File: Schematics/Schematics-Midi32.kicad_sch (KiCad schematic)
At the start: 1 part, among them J1 AudioJack2

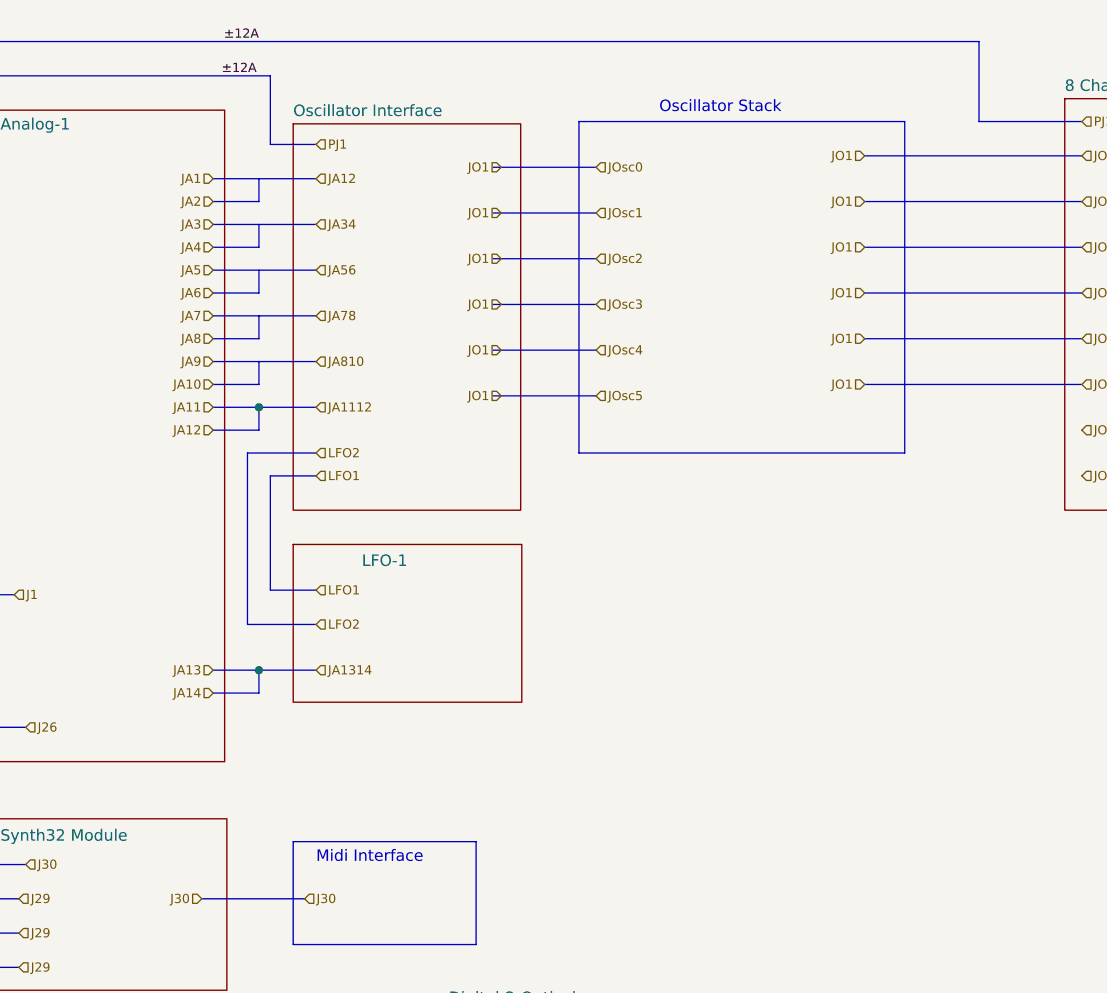
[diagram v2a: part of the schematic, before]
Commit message: Noise generator and experimental steups.
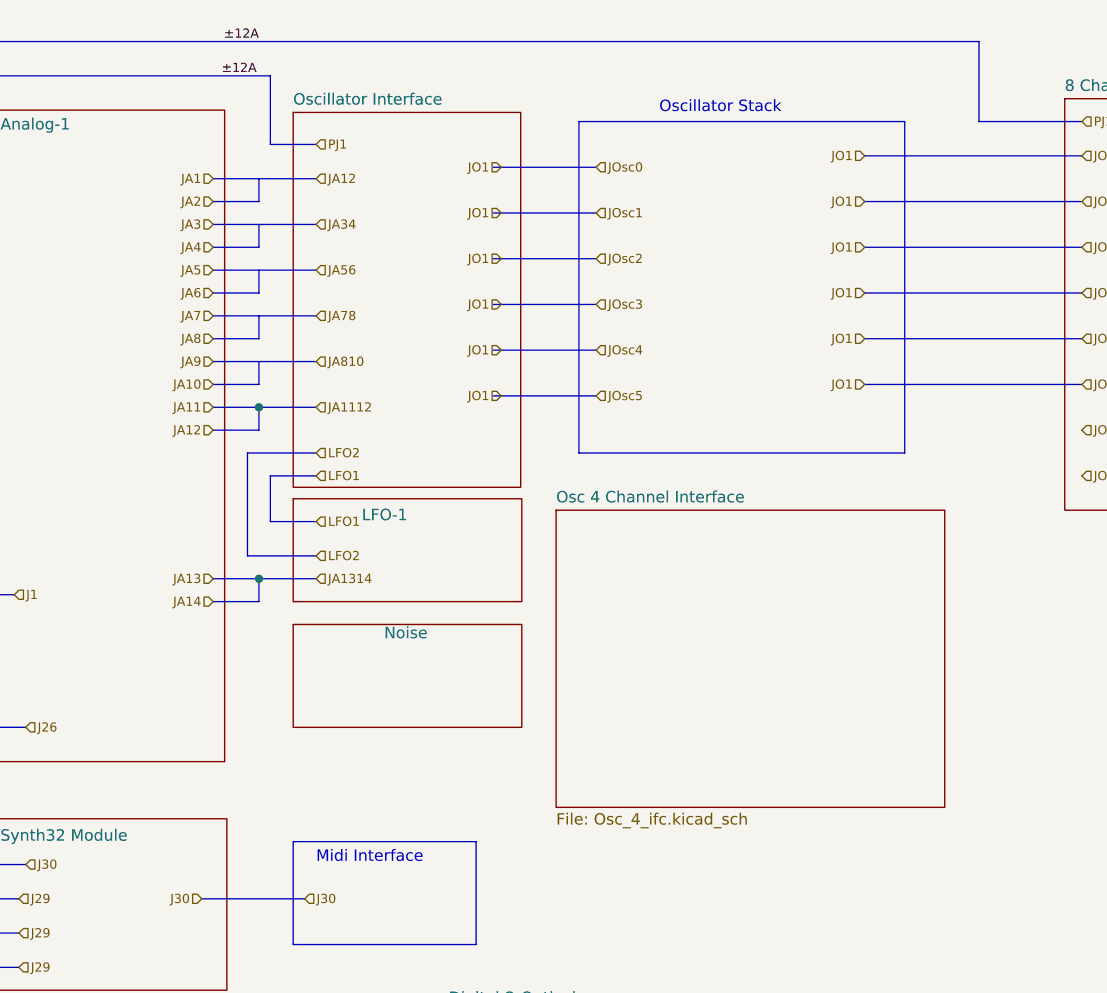
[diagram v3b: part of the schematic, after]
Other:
- added sheet Noise (Noise.kicad_sch)
- added sheet Osc 4 Channel Interface (Osc_4_ifc.kicad_sch)
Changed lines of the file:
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@@
     (comment 2 "In Development")
   )
-  (junction (at 83.82 86.36) (diameter 0) (color 0 0 0 0)
+  (junction (at 83.82 76.2) (diameter 0) (color 0 0 0 0)
   )
   (junction (at 83.82 57.15) (diameter 0) (color 0 0 0 0)
@@
     (stroke (width 0) (type default))
   )
-  (bus (pts (xy 82.55 62.23) (xy 82.55 81.28))
+  (bus (pts (xy 82.55 62.23) (xy 82.55 73.66))
     (stroke (width 0) (type default))
   )
@@
     (stroke (width 0) (type default))
   )
-  (bus (pts (xy 83.82 86.36) (xy 83.82 88.9))
+  (bus (pts (xy 83.82 76.2) (xy 83.82 78.74))
     (stroke (width 0) (type default))
   )
@@
     (stroke (width 0) (type default))
   )
-  (bus (pts (xy 82.55 81.28) (xy 90.17 81.28))
+  (bus (pts (xy 82.55 73.66) (xy 90.17 73.66))
     (stroke (width 0) (type default))
   )
@@
     (stroke (width 0) (type default))
   )
-  (bus (pts (xy 78.74 88.9) (xy 83.82 88.9))
+  (bus (pts (xy 78.74 78.74) (xy 83.82 78.74))
     (stroke (width 0) (type default))
   )
@@
     (stroke (width 0) (type default))
   )
-  (bus (pts (xy 78.74 86.36) (xy 83.82 86.36))
+  (bus (pts (xy 78.74 76.2) (xy 83.82 76.2))
     (stroke (width 0) (type default))
   )
@@
     (stroke (width 0) (type default))
   )
-  (bus (pts (xy 85.09 77.47) (xy 90.17 77.47))
+  (bus (pts (xy 85.09 69.85) (xy 90.17 69.85))
     (stroke (width 0) (type default))
   )
@@
     (stroke (width 0) (type default))
   )
-  (bus (pts (xy 85.09 77.47) (xy 85.09 64.77))
+  (bus (pts (xy 85.09 69.85) (xy 85.09 64.77))
     (stroke (width 0) (type default))
   )
@@
     (stroke (width 0) (type default))
   )
-  (bus (pts (xy 83.82 86.36) (xy 90.17 86.36))
+  (bus (pts (xy 83.82 76.2) (xy 90.17 76.2))
     (stroke (width 0) (type default))
   )
@@
     (effects (font (size 1.016 1.016)) (justify right))
   )
-  (hierarchical_label "JA13" (shape input) (at 78.74 86.36 180) (fields_autoplaced)
+  (hierarchical_label "JA13" (shape input) (at 78.74 76.2 180) (fields_autoplaced)
     (effects (font (size 1.016 1.016)) (justify right))
   )
@@
     (effects (font (size 1.016 1.016)) (justify left))
   )
-  (hierarchical_label "JA1314" (shape input) (at 90.17 86.36 0) (fields_autoplaced)
+  (hierarchical_label "JA1314" (shape input) (at 90.17 76.2 0) (fields_autoplaced)
     (effects (font (size 1.016 1.016)) (justify left))
   )
@@
     (effects (font (size 1.016 1.016)) (justify left))
   )
-  (hierarchical_label "LFO2" (shape input) (at 90.17 81.28 0) (fields_autoplaced)
+  (hierarchical_label "LFO2" (shape input) (at 90.17 73.66 0) (fields_autoplaced)
     (effects (font (size 1.016 1.016)) (justify left))
   )
@@
     (effects (font (size 1.016 1.016)) (justify left))
   )
-  (hierarchical_label "JA14" (shape input) (at 78.74 88.9 180) (fields_autoplaced)
+  (hierarchical_label "JA14" (shape input) (at 78.74 78.74 180) (fields_autoplaced)
     (effects (font (size 1.016 1.016)) (justify right))
   )
@@
     (effects (font (size 1.016 1.016)) (justify left))
   )
-  (hierarchical_label "LFO1" (shape input) (at 90.17 77.47 0) (fields_autoplaced)
+  (hierarchical_label "LFO1" (shape input) (at 90.17 69.85 0) (fields_autoplaced)
     (effects (font (size 1.016 1.016)) (justify left))
   )
@@
     )
   )
-  (sheet (at 87.63 25.654) (size 25.273 42.926) (fields_autoplaced)
-    (stroke (width 0.1524) (type solid))
-    (fill (color 0 0 0 0.0000))
-    (property "Sheetname" "Oscillator Interface" (at 87.63 24.9424 0)
-      (effects (font (size 1.27 1.27)) (justify left bottom))
-    )
-    (property "Sheetfile" "Oscc_6Ifc.kicad_sch" (at 87.63 69.1646 0)
+  (sheet (at 87.63 24.384) (size 25.273 41.656) (fields_autoplaced)
+    (stroke (width 0.1524) (type solid))
+    (fill (color 0 0 0 0.0000))
+    (property "Sheetname" "Oscillator Interface" (at 87.63 23.6724 0)
+      (effects (font (size 1.27 1.27)) (justify left bottom))
+    )
+    (property "Sheetfile" "Oscc_6Ifc.kicad_sch" (at 87.63 66.6246 0)
       (effects (font (size 1.27 1.27)) (justify left top) hide)
     )
@@
       (project "Schematics-Midi32"
         (path "/718f017d-28fe-4e29-b548-40db8e21cec7" (page "7"))
+      )
+    )
+  )
+  (sheet (at 116.84 68.58) (size 43.18 33.02) (fields_autoplaced)
+    (stroke (width 0.1524) (type solid))
+    (fill (color 0 0 0 0.0000))
+    (property "Sheetname" "Osc 4 Channel Interface" (at 116.84 67.8684 0)
+      (effects (font (size 1.27 1.27)) (justify left bottom))
+    )
+    (property "Sheetfile" "Osc_4_ifc.kicad_sch" (at 116.84 102.1846 0)
+      (effects (font (size 1.27 1.27)) (justify left top))
+    )
+    (instances
+      (project "Schematics-Midi32"
+        (path "/718f017d-28fe-4e29-b548-40db8e21cec7" (page "10"))
       )
     )
@@
     )
   )
-  (sheet (at 87.63 72.39) (size 25.4 17.526)
-    (stroke (width 0.1524) (type solid))
-    (fill (color 0 0 0 0.0000))
-    (property "Sheetname" "LFO-1" (at 95.25 74.93 0)
-      (effects (font (size 1.27 1.27)) (justify left bottom))
-    )
-    (property "Sheetfile" "LFO-1.kicad_sch" (at 87.63 91.5166 0)
+  (sheet (at 87.63 67.31) (size 25.4 11.43)
+    (stroke (width 0.1524) (type solid))
+    (fill (color 0 0 0 0.0000))
+    (property "Sheetname" "LFO-1" (at 95.25 69.85 0)
+      (effects (font (size 1.27 1.27)) (justify left bottom))
+    )
+    (property "Sheetfile" "LFO-1.kicad_sch" (at 87.63 86.4366 0)
       (effects (font (size 1.27 1.27)) (justify left top) hide)
     )
@@
       )
     )
+  )
+  (sheet (at 87.63 81.28) (size 25.4 11.43)
+    (stroke (width 0.1524) (type solid))
+    (fill (color 0 0 0 0.0000))
+    (property "Sheetname" "Noise" (at 97.7302 82.9636 0)
+      (effects (font (size 1.27 1.27)) (justify left bottom))
+    )
+    (property "Sheetfile" "Noise.kicad_sch" (at 87.63 85.6746 0)
+      (effects (font (size 1.27 1.27)) (justify left top) hide)
+    )
+    (instances
+      (project "Schematics-Midi32"
+        (path "/718f017d-28fe-4e29-b548-40db8e21cec7" (page "11"))
+      )
+    )

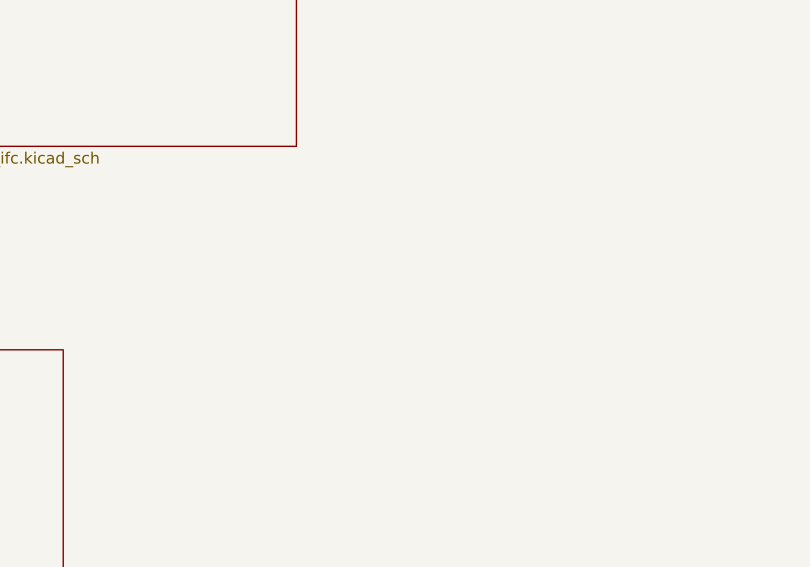
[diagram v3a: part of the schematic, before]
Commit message: adding noise source and variable state filter.
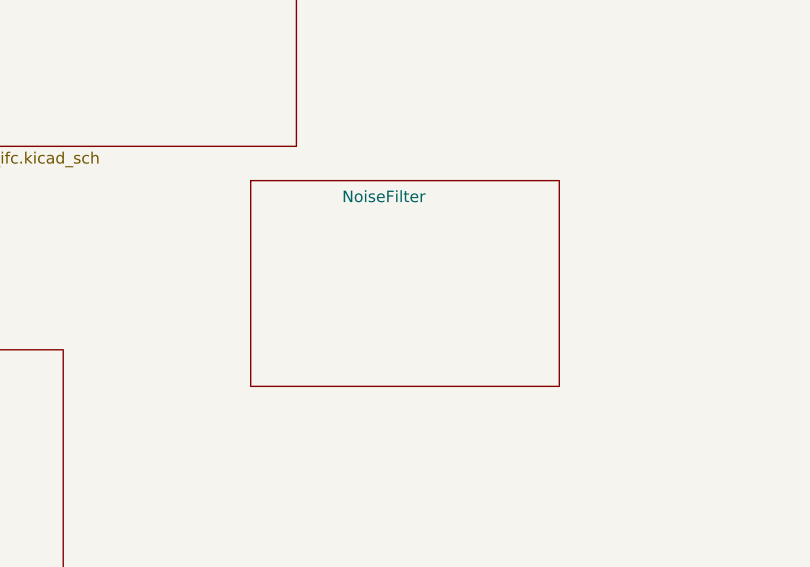
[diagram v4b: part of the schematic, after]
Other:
- added sheet NoiseFilter (NoiseFilter.kicad_sch)
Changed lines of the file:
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@@
+    )
+  )
+  (sheet (at 154.94 105.41) (size 34.29 22.86)
+    (stroke (width 0.1524) (type solid))
+    (fill (color 0 0 0 0.0000))
+    (property "Sheetname" "NoiseFilter" (at 165.1 107.95 0)
+      (effects (font (size 1.27 1.27)) (justify left bottom))
+    )
+    (property "Sheetfile" "NoiseFilter.kicad_sch" (at 154.94 128.8546 0)
+      (effects (font (size 1.27 1.27)) (justify left top) hide)
+    )
+    (instances
+      (project "Schematics-Midi32"
+        (path "/718f017d-28fe-4e29-b548-40db8e21cec7" (page "12"))
+      )
     )
   )

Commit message: sync up first noise board.
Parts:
- added J83: AudioJack2, symbol Connector:AudioJack2
- J1: value AudioJack2 -> AudioJack1
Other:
- sheet 8 Channel Mixer renamed 8 Chan Mixer
- sheet NoiseFilter renamed NoiseFilter-2x  X3
- sheet Osc 4 Channel Interface renamed Osc4 Interface
- sheet Oscillator Interface renamed Osc6 Interface
- note added: "+7 3A"
- note removed: "Midi Interface"
- moved on the sheet: J1

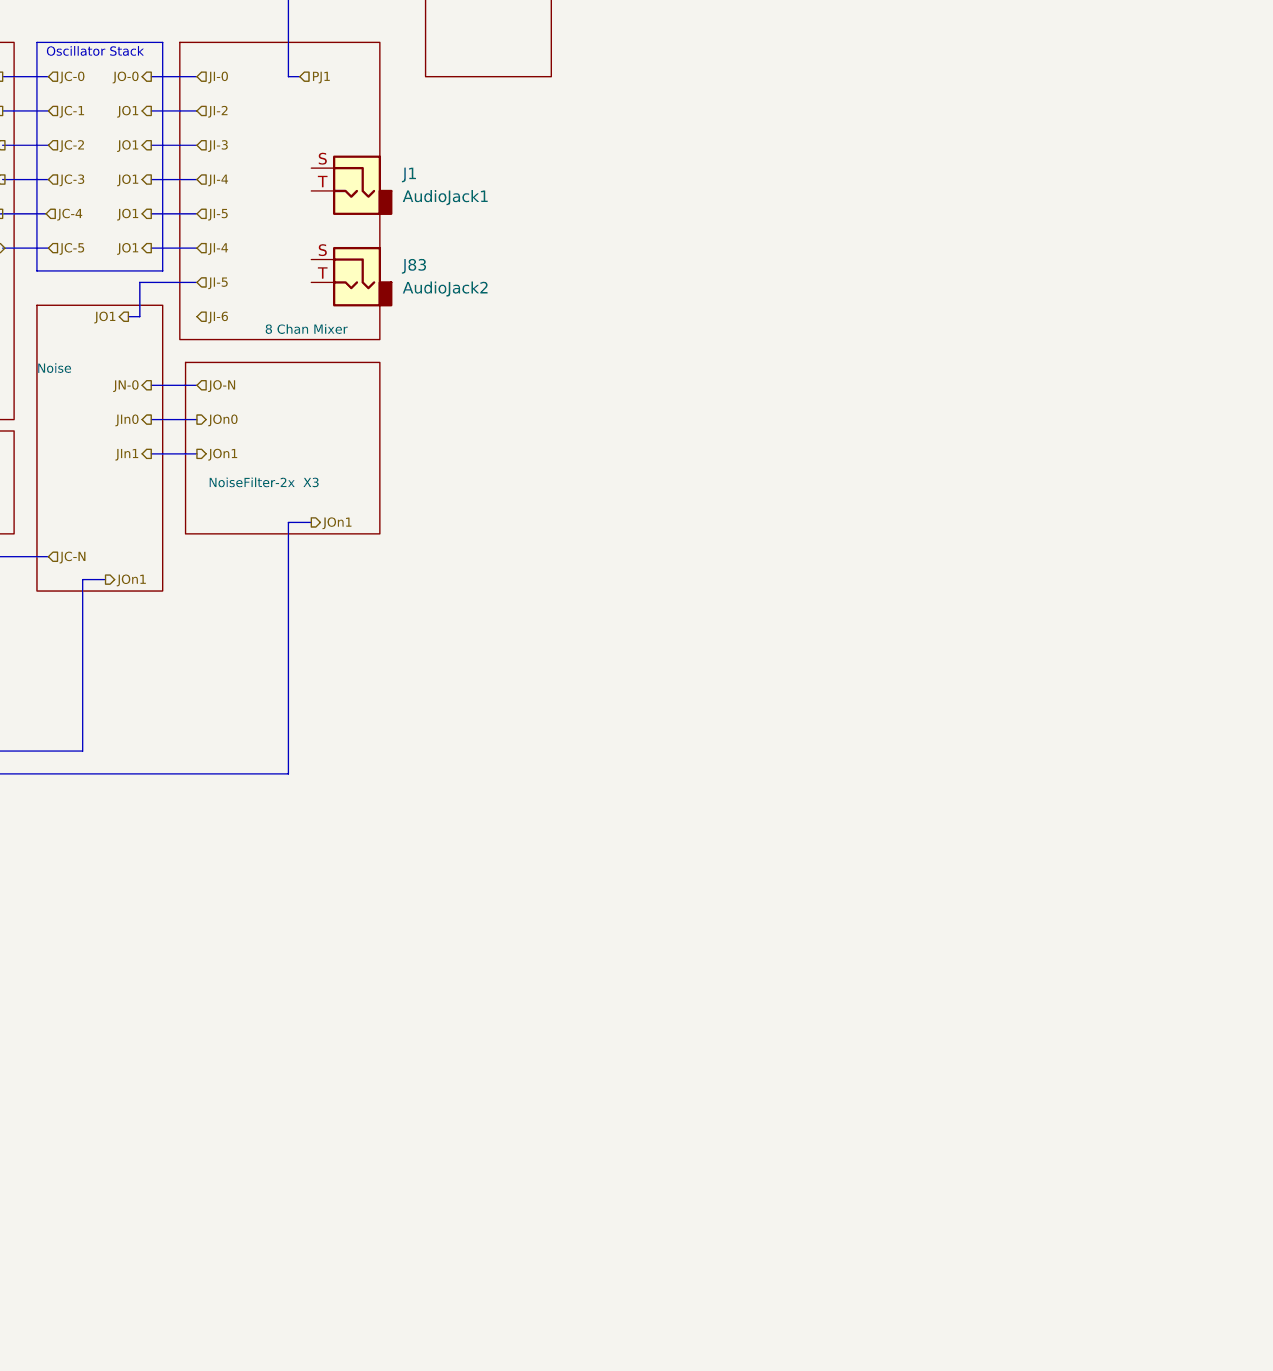
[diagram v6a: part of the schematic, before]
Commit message: Partial software with complete hardware on best 3 state filter with 4 outputs.
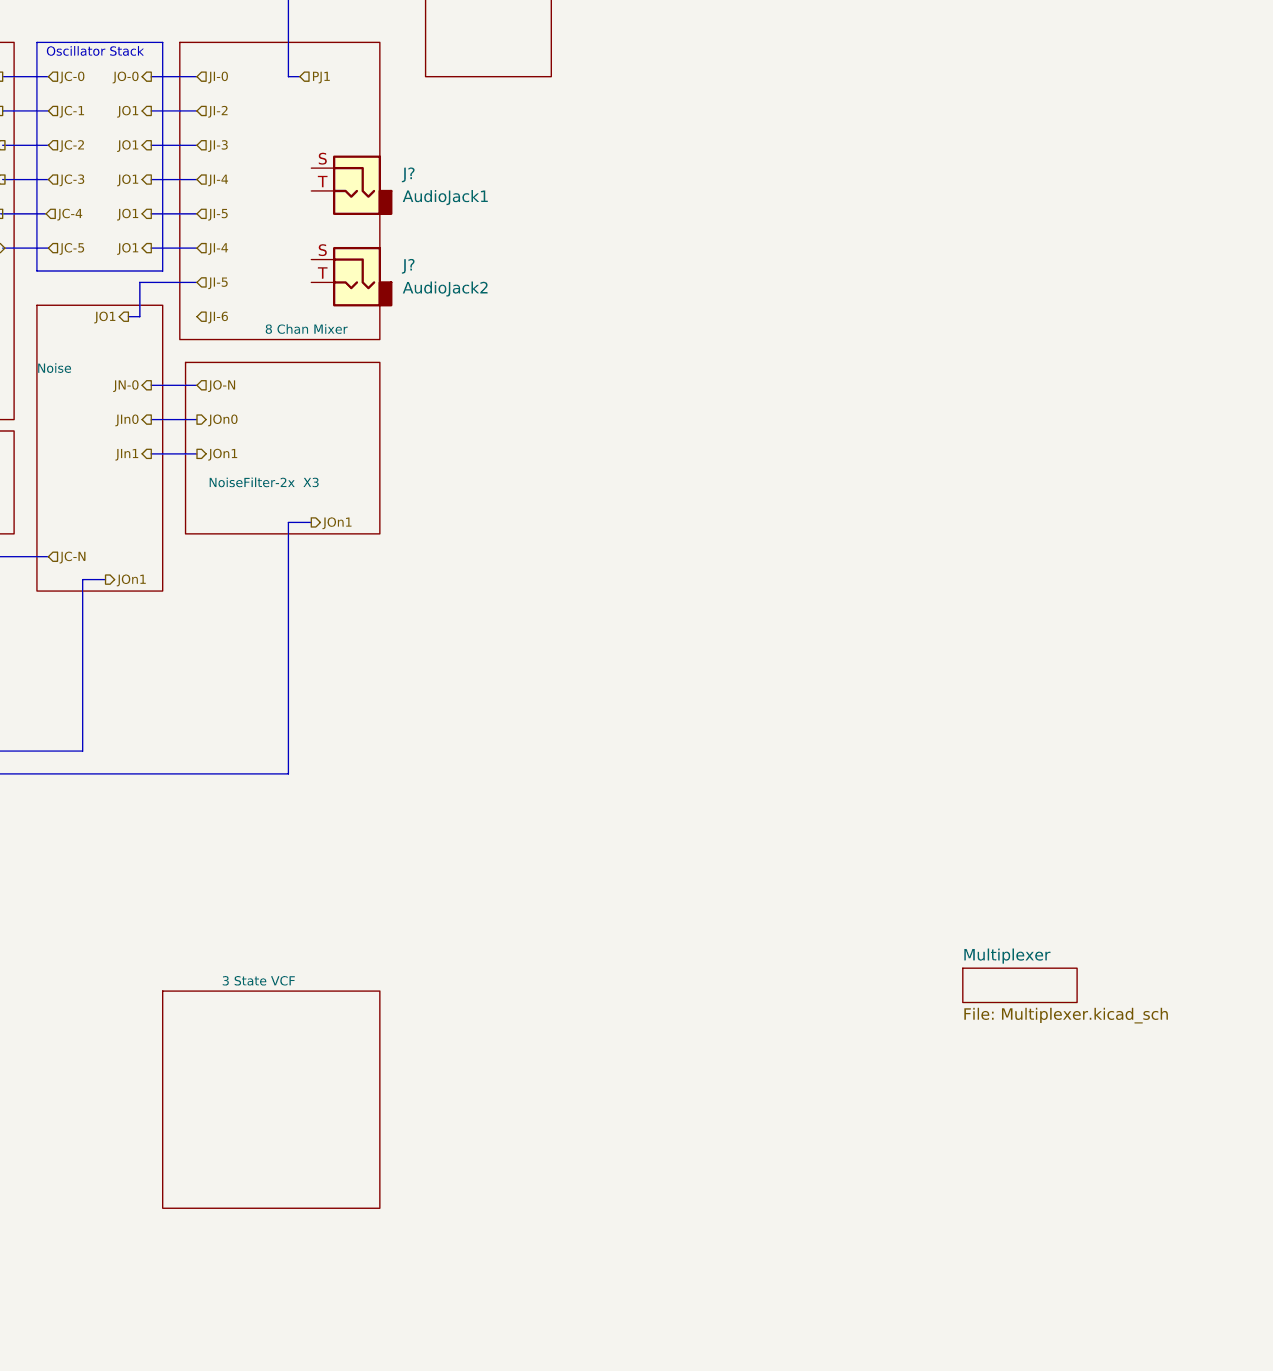
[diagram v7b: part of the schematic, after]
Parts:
- renumbered J83 to J?, J1 to J?
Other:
- added sheet 3 State VCF (3PoleStateVarVCF.kicad_sch)
- added sheet Multiplexer (Multiplexer.kicad_sch)

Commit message: updated schematics.
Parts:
- removed J?: AudioJack2, symbol Connector:AudioJack2
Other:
- sheet 8 Chan Mixer renamed 10 Chan Mixer
- removed sheet NoiseFilter-2x  X3
- removed sheet Osc4 Interface
- removed sheet Osc6 Interface
- added sheet Osc 2 Carrier (Osc2_Carry.kicad_sch)
- note added: "x4"
- note removed: "Oscillator Stack"
- moved on the sheet: J?
